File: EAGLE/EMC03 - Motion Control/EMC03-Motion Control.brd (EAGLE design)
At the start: 150 x 129.9 mm, 205 parts, among them J1 UART0, J10 CPL-CON-HEADER-0.1IN-8P-M, J11 8-PIN HDR, J12 8-PIN HDR, J13 8-PIN HDR, J14 8-PIN HDR, J15 8-PIN HDR, J2 SWD, J3 USB-B, J4 USD-SOCKETSMD, J5 CONN-0.1-RA-1X3, J6 CONN-0.1-RA-1X3, J7 CONN-0.1-RA-1X3, J8 OSTTH050160, J9 CONN-0.1-S-1X2, Q1 TBD, Q2 25MHz, U1 LPC1768, U2 SP3485, U3 CPL-ETH-PHY-LAN8720A, U4 74LVC1G04, U5 74AHCT, U6 TMC2130-LA, U7 TMC2130-LA, U8 TMC2130-LA

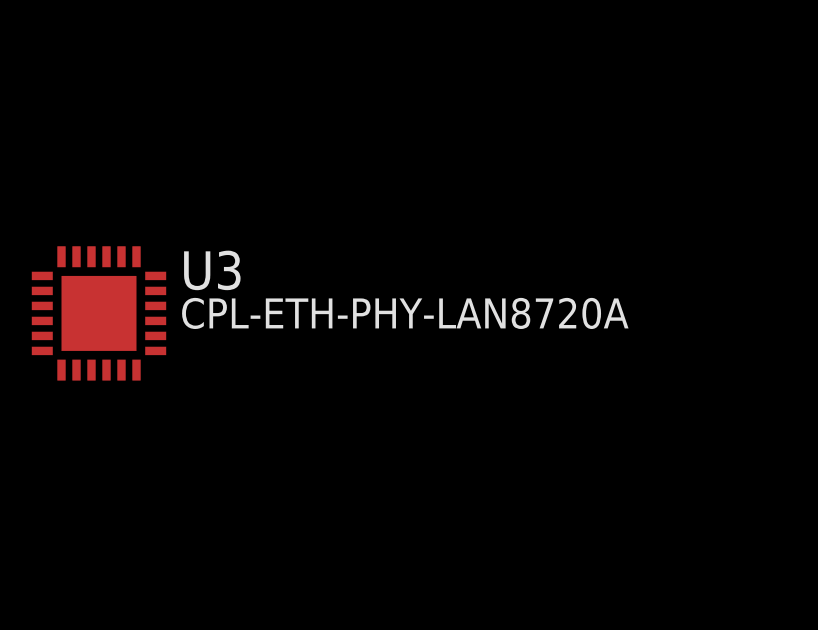
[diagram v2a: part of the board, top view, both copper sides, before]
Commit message: Added a BOM for EMC03, created a checklist for PCB mfr, finalized schematic (rearranged refdes', fixed missing values, etc.)
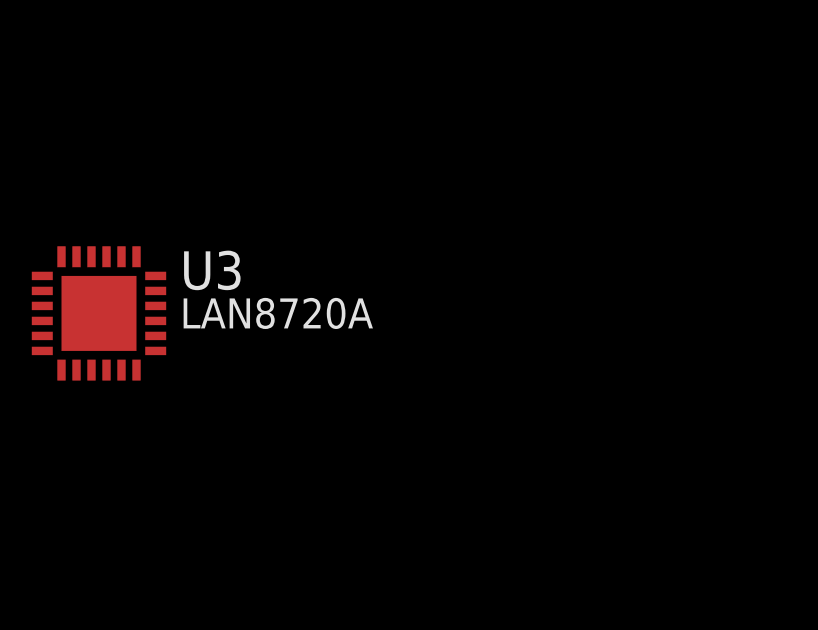
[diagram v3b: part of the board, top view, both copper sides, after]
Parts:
- J10: value CPL-CON-HEADER-0.1IN-8P-M -> 67997-108HLF
- J11, J12, J13, J14, J15: value 8-PIN HDR -> 67997-108HLF
- J4: value USD-SOCKETSMD -> MicroSD
- J5, J6, J7: value CONN-0.1-RA-1X3 -> 68000-103HLF
- J8: value OSTTH050160 -> TBD
- J9: value CONN-0.1-S-1X2 -> 68000-102HLF
- U3: value CPL-ETH-PHY-LAN8720A -> LAN8720A
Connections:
- net !ENABLE: now also U5.4
- net ESTOP_OE: now also U5.1
- net GND: now also U5.3
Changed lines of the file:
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@@
 </autorouter>
 <elements>
-<element name="J6" library="TinWhiskers" package="CON-HDR-3POS-MALE" value="CONN-0.1-RA-1X3" x="17.75" y="40.227" smashed="yes" rot="R300">
+<element name="J6" library="TinWhiskers" package="CON-HDR-3POS-MALE" value="68000-103HLF" x="17.75" y="40.227" smashed="yes" rot="R300">
 <attribute name="NAME" x="13.02494375" y="44.25180625" size="1.5" layer="25" ratio="10" rot="R30"/>
 <attribute name="PARTNO" value="CONN-0.1-RA-1X3" x="17.75" y="40.227" size="1.778" layer="27" rot="R300" display="off"/>
 </element>
-<element name="J5" library="TinWhiskers" package="CON-HDR-3POS-MALE" value="CONN-0.1-RA-1X3" x="94.5" y="126.603" smashed="yes" rot="R180">
+<element name="J5" library="TinWhiskers" package="CON-HDR-3POS-MALE" value="68000-103HLF" x="94.5" y="126.603" smashed="yes" rot="R180">
 <attribute name="NAME" x="101.949" y="126.593" size="1.5" layer="25" ratio="10" rot="R90"/>
 <attribute name="PARTNO" value="CONN-0.1-RA-1X3" x="94.5" y="126.603" size="1.778" layer="27" rot="R180" display="off"/>
 </element>
-<element name="J7" library="TinWhiskers" package="CON-HDR-3POS-MALE" value="CONN-0.1-RA-1X3" x="125.056" y="27.745" smashed="yes" rot="R60">
+<element name="J7" library="TinWhiskers" package="CON-HDR-3POS-MALE" value="68000-103HLF" x="125.056" y="27.745" smashed="yes" rot="R60">
 <attribute name="NAME" x="123.606059375" y="21.498190625" size="1.5" layer="25" ratio="10" rot="R150"/>
 <attribute name="PARTNO" value="CONN-0.1-RA-1X3" x="125.056" y="27.745" size="1.778" layer="27" rot="R60" display="off"/>
@@
 <attribute name="PARTNO" value="CC0805ZRY5V9BB104" x="82.25" y="36.202" size="1.778" layer="27" display="off"/>
 </element>
-<element name="J9" library="TinWhiskers" package="CON-HDR-2POS-MALE" value="CONN-0.1-S-1X2" x="75" y="2.702" smashed="yes">
+<element name="J9" library="TinWhiskers" package="CON-HDR-2POS-MALE" value="68000-102HLF" x="75" y="2.702" smashed="yes">
 <attribute name="NAME" x="78.21" y="3.103" size="1.2" layer="25" ratio="10"/>
 <attribute name="PARTNO" value="CONN-0.1-S-1X2" x="75" y="2.702" size="1.778" layer="27" display="off"/>
@@
 <attribute name="BOM" value="EXCLUDE" x="108" y="122.11" size="1.778" layer="27" display="off"/>
 </element>
-<element name="J8" library="TinWhiskers" package="CON-HDR-6POS-MALE" value="OSTTH050160" x="75" y="125.952" smashed="yes">
+<element name="J8" library="TinWhiskers" package="CON-HDR-6POS-MALE" value="TBD" x="75" y="125.952" smashed="yes">
 <attribute name="PARTNO" value="OSTTH050160" x="75" y="125.952" size="1.778" layer="27" display="off"/>
 </element>
@@
 <element name="S3" library="TinWhiskers" package="0603" value="147873-2" x="129.904" y="-389.712"/>
 <element name="R5" library="TinWhiskers" package="R0603" value="10k" x="324.76" y="-194.856"/>
-<element name="U3" library="TinWhiskers" package="QFN-24" value="CPL-ETH-PHY-LAN8720A" x="714.472" y="-64.952"/>
+<element name="U3" library="TinWhiskers" package="QFN-24" value="LAN8720A" x="714.472" y="-64.952"/>
 <element name="R10" library="TinWhiskers" package="R0603" value="22R" x="324.76" y="194.856"/>
 <element name="R11" library="TinWhiskers" package="R0603" value="22R" x="389.712" y="194.856"/>
@@
 <element name="R33" library="TinWhiskers" package="R0603" value="330R" x="584.568" y="259.808"/>
 <element name="R34" library="TinWhiskers" package="R0603" value="330R" x="649.52" y="259.808"/>
-<element name="J4" library="TinWhiskers" package="MICRO-SD-SOCKET-PP" value="USD-SOCKETSMD" x="324.76" y="324.76"/>
+<element name="J4" library="TinWhiskers" package="MICRO-SD-SOCKET-PP" value="MicroSD" x="324.76" y="324.76"/>
 <element name="C33" library="TinWhiskers" package="C0603" value="1uF" x="519.616" y="-64.952"/>
 <element name="C34" library="TinWhiskers" package="C0603" value="0.1uF" x="519.616" y="0"/>
@@
 <element name="C48" library="TinWhiskers" package="C0603" value="100nF" x="-64.952" y="454.664"/>
 <element name="C49" library="TinWhiskers" package="C0603" value="22 nF" x="0" y="454.664"/>
-<element name="J11" library="TinWhiskers" package="CON-HDR-8POS-MALE" value="8-PIN HDR" x="64.952" y="194.856"/>
-<element name="J10" library="TinWhiskers" package="CON-HDR-8POS-MALE" value="CPL-CON-HEADER-0.1IN-8P-M" x="129.904" y="194.856"/>
+<element name="J11" library="TinWhiskers" package="CON-HDR-8POS-MALE" value="67997-108HLF" x="64.952" y="194.856"/>
+<element name="J10" library="TinWhiskers" package="CON-HDR-8POS-MALE" value="67997-108HLF" x="129.904" y="194.856"/>
 <element name="C50" library="TinWhiskers" package="C0603" value="0.33uF" x="194.856" y="324.76"/>
 <element name="C51" library="TinWhiskers" package="C0603" value="100 nF" x="129.904" y="324.76"/>
@@
 <element name="C58" library="TinWhiskers" package="C0603" value="100nF" x="-389.712" y="194.856"/>
 <element name="C59" library="TinWhiskers" package="C0603" value="22 nF" x="-324.76" y="194.856"/>
-<element name="J14" library="TinWhiskers" package="CON-HDR-8POS-MALE" value="8-PIN HDR" x="129.904" y="519.616"/>
+<element name="J14" library="TinWhiskers" package="CON-HDR-8POS-MALE" value="67997-108HLF" x="129.904" y="519.616"/>
 <element name="C60" library="TinWhiskers" package="C0603" value="0.33uF" x="-129.904" y="64.952"/>
 <element name="C61" library="TinWhiskers" package="C0603" value="100 nF" x="-194.856" y="64.952"/>
@@
 <element name="C71" library="TinWhiskers" package="C0603" value="100nF" x="-389.712" y="519.616"/>
 <element name="C72" library="TinWhiskers" package="C0603" value="22 nF" x="-324.76" y="519.616"/>
-<element name="J13" library="TinWhiskers" package="CON-HDR-8POS-MALE" value="8-PIN HDR" x="-259.808" y="259.808"/>
-<element name="J12" library="TinWhiskers" package="CON-HDR-8POS-MALE" value="8-PIN HDR" x="-194.856" y="259.808"/>
+<element name="J13" library="TinWhiskers" package="CON-HDR-8POS-MALE" value="67997-108HLF" x="-259.808" y="259.808"/>
+<element name="J12" library="TinWhiskers" package="CON-HDR-8POS-MALE" value="67997-108HLF" x="-194.856" y="259.808"/>
 <element name="C73" library="TinWhiskers" package="C0603" value="0.33uF" x="-129.904" y="389.712"/>
 <element name="C74" library="TinWhiskers" package="C0603" value="100 nF" x="-194.856" y="389.712"/>
@@
 <element name="R8" library="TinWhiskers" package="R0603" value="470R" x="-64.952" y="-259.808"/>
 <element name="R9" library="TinWhiskers" package="R0603" value="470R" x="-64.952" y="-324.76"/>
-<element name="J15" library="TinWhiskers" package="CON-HDR-8POS-MALE" value="8-PIN HDR" x="0" y="-389.712"/>
+<element name="J15" library="TinWhiskers" package="CON-HDR-8POS-MALE" value="67997-108HLF" x="0" y="-389.712"/>
 <element name="U5" library="TinWhiskers" package="SC70" value="74AHCT" x="0" y="0"/>
 <element name="Q1" library="TinWhiskers" package="HC-49/U-S" value="TBD" x="-454.664" y="454.664"/>
@@
 <contactref element="VR3" pad="2"/>
 <contactref element="VR5" pad="2"/>
+<contactref element="U5" pad="3"/>
 <wire x1="73.882" y1="194.856" x2="58.612" y2="194.856" width="0" layer="19" extent="1-1"/>
 <wire x1="77.1" y1="128.503" x2="73.882" y2="194.856" width="0" layer="19" extent="1-1"/>
@@
 <wire x1="100.65" y1="3.153" x2="115.35" y2="12.077" width="0" layer="19" extent="1-1"/>
 <wire x1="90.525" y1="3.653" x2="100.65" y2="3.153" width="0" layer="19" extent="1-1"/>
+<wire x1="-0.65" y1="1.1" x2="30.3" y2="19.627" width="0" layer="19" extent="1-1"/>
+<wire x1="-64.952" y1="-61.457" x2="-0.65" y2="1.1" width="0" layer="19" extent="1-1"/>
+<wire x1="-64.952" y1="-73.082" x2="-64.952" y2="-61.457" width="0" layer="19" extent="1-1"/>
+<wire x1="-61.552" y1="-73.082" x2="-64.952" y2="-73.082" width="0" layer="19" extent="1-1"/>
+<wire x1="-64.952" y1="-134.0665" x2="-64.952" y2="-73.082" width="0" layer="19" extent="1-1"/>
 <wire x1="193.606" y1="192.056" x2="114.4" y2="122.528" width="0" layer="19" extent="1-1"/>
 <wire x1="196.606" y1="192.056" x2="193.606" y2="192.056" width="0" layer="19" extent="1-1"/>
@@
 <wire x1="193.606" y1="197.656" x2="194.856" y2="194.856" width="0" layer="19" extent="1-1"/>
 <wire x1="193.106" y1="197.656" x2="193.606" y2="197.656" width="0" layer="19" extent="1-1"/>
-<wire x1="-64.952" y1="-61.457" x2="35.85" y2="7.603" width="0" layer="19" extent="1-1"/>
-<wire x1="-64.952" y1="-73.082" x2="-64.952" y2="-61.457" width="0" layer="19" extent="1-1"/>
-<wire x1="-61.552" y1="-73.082" x2="-64.952" y2="-73.082" width="0" layer="19" extent="1-1"/>
-<wire x1="-64.952" y1="-134.0665" x2="-64.952" y2="-73.082" width="0" layer="19" extent="1-1"/>
 <wire x1="194.131" y1="324.76" x2="193.606" y2="197.656" width="0" layer="19" extent="1-1"/>
 <wire x1="129.179" y1="324.76" x2="194.131" y2="324.76" width="0" layer="19" extent="1-1"/>
@@
 <contactref element="U6" pad="22"/>
 <contactref element="J10" pad="1"/>
+<contactref element="U5" pad="4"/>
 <wire x1="121.014" y1="519.616" x2="197.156" y2="518.866" width="0" layer="19" extent="1-1"/>
-<wire x1="-203.746" y1="259.808" x2="121.014" y2="519.616" width="0" layer="19" extent="1-1"/>
-<wire x1="-127.604" y1="259.058" x2="-203.746" y2="259.808" width="0" layer="19" extent="1-1"/>
 <wire x1="197.156" y1="194.106" x2="197.156" y2="518.866" width="0" layer="19" extent="1-1"/>
 <wire x1="121.014" y1="194.856" x2="197.156" y2="194.106" width="0" layer="19" extent="1-1"/>
 <wire x1="72.75" y1="36.452" x2="121.014" y2="194.856" width="0" layer="19" extent="1-1"/>
+<wire x1="-0.65" y1="-1.1" x2="46.69281875" y2="41.102" width="0" layer="19" extent="1-1"/>
+<wire x1="-127.604" y1="259.058" x2="121.014" y2="194.856" width="0" layer="19" extent="1-1"/>
+<wire x1="-203.746" y1="259.808" x2="-127.604" y2="259.058" width="0" layer="19" extent="1-1"/>
 </signal>
 <signal name="Z_MIN">
@@
 <wire x1="74" y1="54.952" x2="70.035" y2="54.952" width="0.3" layer="1"/>
 <wire x1="70.035" y1="54.952" x2="70" y2="54.917" width="0.3" layer="1"/>
+<contactref element="U5" pad="1"/>
+<wire x1="0.65" y1="1.1" x2="70" y2="14.452" width="0" layer="19" extent="1-16"/>
 </signal>
 <signal name="N$5">

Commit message: Modified the BOM to reflect connector, resonator changes. All component parts for EBR01 and their equivalents on EMC03 were ordered and the BOMs were updated to reflect this. The database for the new BOM-EX extension for EAGLE was updated to include all relevant parts and debugged for future use. A preliminary choice for power connector has been made.
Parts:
- added C76: 0.47uF, TinWhiskers:C0603
- C2, C4: device SparkFun-Capacitors:0805 -> TinWhiskers:C0603
- FB1: value BLM15HBK1608H220-T0603 -> BLM18AG121SN1D
- FB2: value BK1608H220-T -> BLM18AG121SN1D
- R19, R20, R21, R27, R29: device SparkFun-Resistors:0805 -> TinWhiskers:R0603
- U4: value 74LVC1G04 -> 74LVC1G04W5-7
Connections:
- removed net VSW_IN: C37.POS, J8.2, VR2.1
- new net N$4: C76.2, VR2.5
- net +24V: now also C37.POS, VR2.1
- net GND: now also C76.1; no longer VR2.5

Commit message: Updated BOM, Database, Schematic for final parts
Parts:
- removed J13, J14, J15: 67997-108HLF, TinWhiskers:CON-HDR-8POS-MALE
- J10, J11, J12: value 67997-108HLF -> S4B-PH-SM4; device TinWhiskers:CON-HDR-8POS-MALE -> TinWhiskers:CONN-JST-PH-2.0MM-4P-SMT-RA
- J5, J6, J7: value 68000-103HLF -> S3B-PH-SM4; device TinWhiskers:CON-HDR-3POS-MALE -> TinWhiskers:CONN-JST-PH-2.0MM-3P-SMT-RA
- moved J11 1156.4 mm to (-649.5, -714.5)
- moved J10 1102.3 mm to (-649.5, -584.6)
- moved J12 1016.7 mm to (-649.5, -649.5)
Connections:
- removed net !RESET!: J10.5
- removed net !SLEEP!: J10.6
- removed net MS1: J10.2
- removed net MS2: J10.3
- removed net MS3: J10.4
- removed net VBAT: U1.19
- net !ENABLE: no longer J10.1, J12.1, J14.1
- net +3V3: now also U1.19
- net 1A_1: now also J10.3; no longer J11.5
- net 1A_2: now also J11.3; no longer J13.5
- net 1A_3: now also J12.3; no longer J15.5
- net 1B_1: now also J10.4; no longer J11.6
- net 1B_2: now also J11.4; no longer J13.6
- net 1B_3: now also J12.4; no longer J15.6
- net 2A_1: now also J10.2; no longer J11.4
- net 2A_2: now also J11.2; no longer J13.4
- net 2A_3: now also J12.2; no longer J15.4
- net 2B_1: now also J10.1; no longer J11.3
- net 2B_2: now also J11.1; no longer J13.3
- net 2B_3: now also J12.1; no longer J15.3
- net GND: no longer J11.2, J11.8, J13.2, J13.8, J15.2, J15.8
- net X_DIR: no longer J10.8
- net X_STEP: no longer J10.7
- net Y_DIR: no longer J12.8
- net Y_STEP: no longer J12.7
- net Z_DIR: no longer J14.8
- net Z_STEP: no longer J14.7
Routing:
- net Y_STOP: track 70.3 -> 77.1 mm
- net X_STOP: track 5.40 -> 8.69 mm
- net Z_STOP: track 2.35 -> 4.64 mm

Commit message: EMC03: Updated schematic, BOM, database, and parts library to include all revisions. This includes schematic capture for interfaces (endstops, motors, encoders, RS-485 interface, modular tools 1 and 2, the up-looking camera, the end effector the SWD connector, and the power jack).
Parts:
- removed RJ2: HR911105A, TinWhiskers:MAGJACK(HR911105A)
- added J13, J14, J15: S5B-PH-SM4, TinWhiskers:CONN-JST-PH-2.0MM-5P-SMT-RA
- added J16, J17: S8B-PH-SM4, TinWhiskers:CONN-JST-PH-2.0MM-8P-SMT-RA
- added J18, J19: S6B-PH-SM4, TinWhiskers:CONN-JST-PH-2.0MM-6P-SMT-RA
- J2: value SWD -> FTSH-105-1-L-DV
- J8: value TBD -> 694106106102; device TinWhiskers:CON-HDR-6POS-MALE -> TinWhiskers:PJ-694106106102
- RJ1: value RJ-45 -> HR911105A; device TinWhiskers:CON-RJ45 -> TinWhiskers:MAGJACK(HR911105A)
- moved J8 1598.6 mm to (-649.5, -1299.0)
- moved RJ1 129.9 mm to (389.7, 324.8)
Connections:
- new net EE_D+: J16.7
- new net EE_D-: J16.8
- new net ENCX_A: J13.2
- new net ENCX_B: J13.3
- new net ENCY_B: J14.3
- new net ENCZ_A: J15.2
- new net ENCZ_B: J15.3
- new net ENXY_A: J14.2
- new net ULC_D+: J17.7
- new net ULC_D-: J17.8
- new net X_INDEX: J13.4
- new net Y_INDEX: J14.4
- new net Z_INDEX: J15.4
- net !ENABLE: now also J16.2, J17.2, J18.2, J19.2
- net +24V: now also J16.1, J17.1, J18.1, J19.1, J8.2; no longer J8.1
- net +5V: now also J13.1, J14.1, J15.1, J16.6, J17.6, J18.6, J19.6
- net A: now also J16.4, J17.4, J18.4, J19.4; no longer RJ1.5
- net B: now also J16.5, J17.5, J18.5, J19.5; no longer RJ1.4
- net GND: now also J13.5, J14.5, J15.5, J16.3, J17.3, J18.3, J19.3, RJ1.SHLD0, RJ1.SHLD1; no longer RJ1.6, RJ2.SHLD0, RJ2.SHLD1
- net LED1/REGOFF: now also RJ1.9; no longer RJ2.9
- net LED2/NINTSEL: now also RJ1.12; no longer RJ2.12
- net N$6: now also RJ1.4, RJ1.5; no longer RJ2.4, RJ2.5
- net N$7: now also RJ1.11; no longer RJ2.11
- net N$8: now also RJ1.10; no longer RJ2.10
- net RD+: now also RJ1.3; no longer RJ2.3
- net RD-: now also RJ1.6; no longer RJ2.6
- net TD+: now also RJ1.1; no longer RJ2.1
- net TD-: now also RJ1.2; no longer RJ2.2
